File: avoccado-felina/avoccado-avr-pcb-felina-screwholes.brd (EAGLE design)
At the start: 44 x 17.5 mm, 80 parts, among them Q1 16MHz, Q2 FET, U1 MPU-6000QFN-24, U2 MCP73831

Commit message: add redundant fiducials near mounting holes, reverse LED and R
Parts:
- added FID5, FID6, FID7, FID8, FID9: FIDUCIALUFIDUCIAL, SparkFun-Aesthetics:MICRO-FIDUCIAL
- moved FID4 44.7 mm to (2.41, 24.5)
- moved R9 3.05 mm to (40.0, 25.1)
- moved D2 2.41 mm to (42.9, 25.0)
- moved FID1 1.27 mm to (2.41, 39.5)
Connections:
- net 5V: now also D2.A; no longer R9.2
- net GND: now also R9.1; no longer D2.C
- net N$3: now also D2.C, R9.2; no longer D2.A, R9.1
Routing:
- net 3.3V: track 167.2 -> 172.3 mm, vias 3 -> 4
- net VBAT: track 35.2 -> 37.1 mm
- net A5: track 20.9 -> 20.2 mm
- net GND: track 212.7 -> 212.2 mm
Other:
- board text added: "DT"
- board text added: "GN"
- board text added: "LIPO"
- board text added: "RX"
- board text added: "TX"
- board text removed: "BAT"
- board text removed: "D"
- board text removed: "R"
- board text removed: "T"

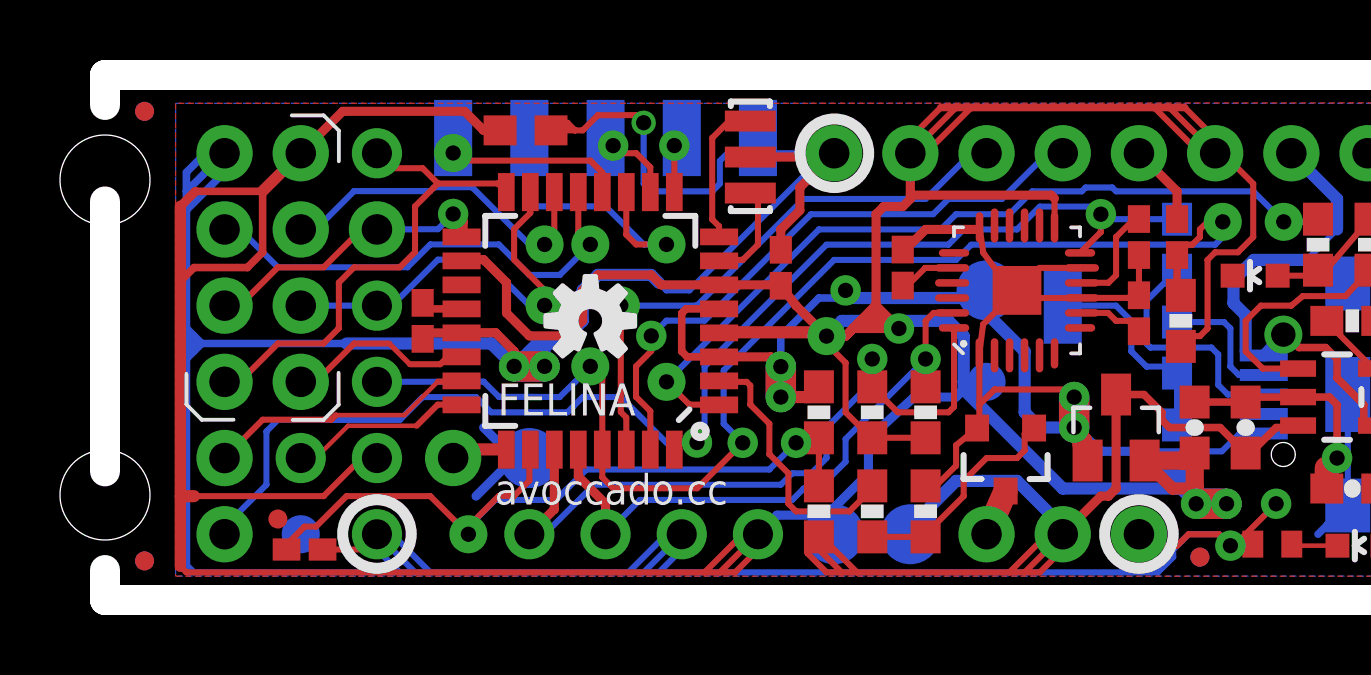
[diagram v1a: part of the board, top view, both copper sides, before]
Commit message: increase trace width for Vcc near edges
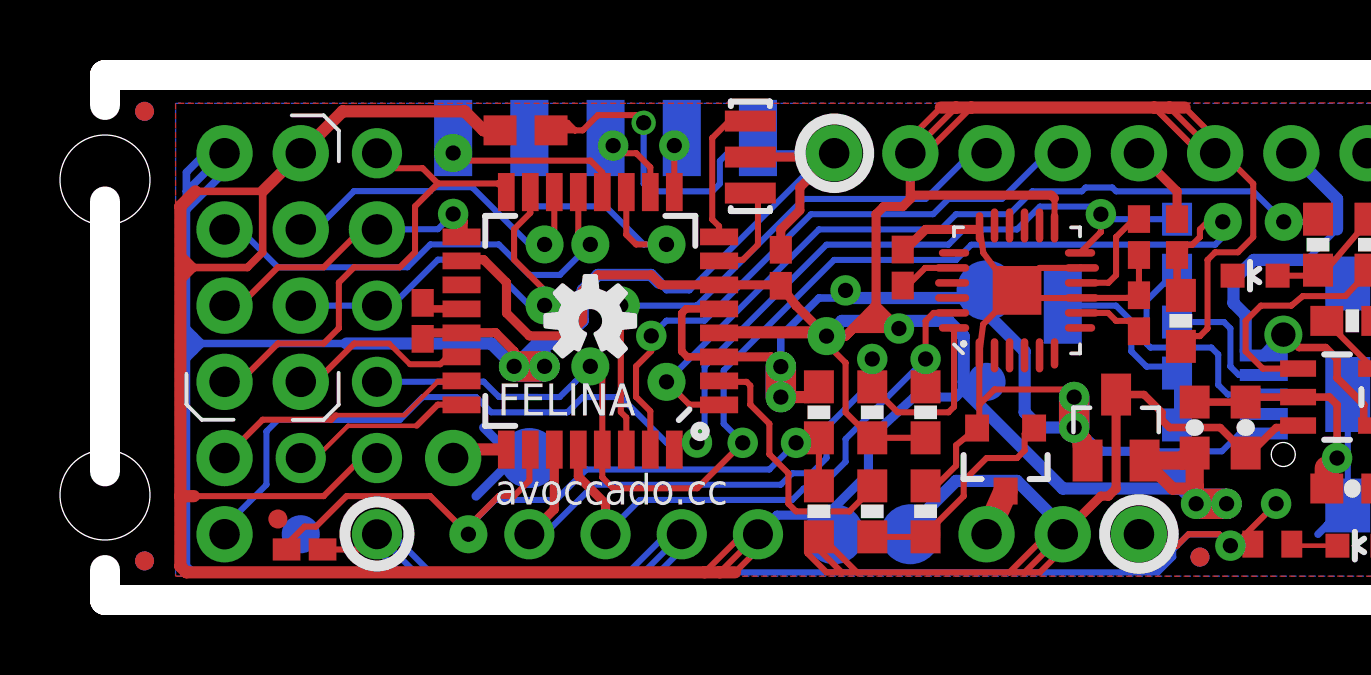
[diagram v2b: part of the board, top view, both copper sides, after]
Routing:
- net 3.3V: track 172.3 -> 173.8 mm
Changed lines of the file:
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@@
 <layer number="22" name="bPlace" color="7" fill="1" visible="yes" active="yes"/>
 <layer number="23" name="tOrigins" color="15" fill="1" visible="yes" active="yes"/>
-<layer number="24" name="bOrigins" color="15" fill="1" visible="yes" active="yes"/>
+<layer number="24" name="bOrigins" color="15" fill="1" visible="no" active="yes"/>
 <layer number="25" name="tNames" color="7" fill="1" visible="no" active="yes"/>
 <layer number="26" name="bNames" color="7" fill="1" visible="no" active="yes"/>
@@
 <layer number="28" name="bValues" color="7" fill="1" visible="no" active="yes"/>
 <layer number="29" name="tStop" color="7" fill="3" visible="yes" active="yes"/>
-<layer number="30" name="bStop" color="7" fill="6" visible="yes" active="yes"/>
-<layer number="31" name="tCream" color="7" fill="4" visible="no" active="yes"/>
-<layer number="32" name="bCream" color="7" fill="5" visible="yes" active="yes"/>
+<layer number="30" name="bStop" color="7" fill="6" visible="no" active="yes"/>
+<layer number="31" name="tCream" color="7" fill="4" visible="yes" active="yes"/>
+<layer number="32" name="bCream" color="7" fill="5" visible="no" active="yes"/>
 <layer number="33" name="tFinish" color="6" fill="3" visible="yes" active="yes"/>
 <layer number="34" name="bFinish" color="6" fill="6" visible="yes" active="yes"/>
@@
 <wire x1="4.326" y1="29.21" x2="5.35" y2="29.21" width="0.127" layer="22"/>
 <rectangle x1="13.208" y1="28.448" x2="21.336" y2="36.576" layer="41"/>
-<circle x="20.32" y="25.408" radius="1.143" width="0.3683" layer="22"/>
+<circle x="20.32" y="25.408" radius="1.0668" width="0.3683" layer="22"/>
 <text x="33.613759375" y="28.141603125" size="1.778" layer="22" font="vector" ratio="15" rot="MR0" align="top-left">+</text>
 <text x="38.956" y="36.576" size="1.016" layer="22" ratio="15" rot="SMR0" align="top-left">VC</text>
@@
 <circle x="25.4" y="38.108" radius="1.143" width="0.3683" layer="22"/>
 <circle x="35.56" y="25.408" radius="1.143" width="0.3683" layer="21"/>
-<circle x="10.16" y="25.408" radius="1.143" width="0.3683" layer="22"/>
-<circle x="10.16" y="25.408" radius="1.143" width="0.3683" layer="21"/>
+<circle x="10.16" y="25.408" radius="1.0668" width="0.3683" layer="22"/>
+<circle x="10.16" y="25.408" radius="1.0668" width="0.3683" layer="21"/>
 <circle x="7.62" y="25.408" radius="0.8128" width="0.3683" layer="22"/>
 <circle x="30.48" y="33.528" radius="1.143" width="0.3683" layer="22"/>
@@
 <wire x1="6.35" y1="36.838" x2="6.35" y2="36.83" width="0.254" layer="1"/>
 <wire x1="6.35" y1="36.83" x2="4.1068" y2="36.83" width="0.254" layer="1"/>
-<wire x1="4.1068" y1="36.83" x2="3.6068" y2="36.33" width="0.3048" layer="1"/>
-<wire x1="3.6068" y1="36.33" x2="3.6068" y2="26.67" width="0.381" layer="1"/>
+<wire x1="4.1068" y1="36.83" x2="3.6068" y2="36.33" width="0.4064" layer="1"/>
+<wire x1="3.6068" y1="36.33" x2="3.6068" y2="26.67" width="0.4064" layer="1"/>
 <contactref element="C6" pad="1"/>
 <contactref element="JP18" pad="1"/>
 <contactref element="JP2" pad="2"/>
-<wire x1="3.6068" y1="26.67" x2="3.6068" y2="24.3332" width="0.381" layer="1"/>
+<wire x1="3.6068" y1="26.67" x2="3.6068" y2="24.3332" width="0.4064" layer="1"/>
 <contactref element="MCU" pad="4"/>
 <contactref element="MCU" pad="6"/>
@@
 <wire x1="6.35" y1="36.83" x2="6.35" y2="34.798" width="0.254" layer="1"/>
 <wire x1="6.35" y1="34.798" x2="5.842" y2="34.29" width="0.254" layer="1"/>
-<wire x1="5.842" y1="34.29" x2="4.064" y2="34.29" width="0.254" layer="1"/>
-<wire x1="4.064" y1="34.29" x2="3.556" y2="33.782" width="0.254" layer="1"/>
-<wire x1="3.556" y1="33.782" x2="3.556" y2="33.528" width="0.254" layer="1"/>
 <contactref element="TP5" pad="P$1"/>
 <wire x1="21.5646" y1="33.712" x2="21.6346" y2="33.782" width="0.254" layer="1"/>
@@
 <wire x1="27.94" y1="36.703" x2="32.639" y2="36.703" width="0.3048" layer="1"/>
 <wire x1="32.639" y1="36.703" x2="32.746" y2="36.596" width="0.3048" layer="1"/>
-<wire x1="3.6068" y1="24.3332" x2="3.81" y2="24.13" width="0.2032" layer="1"/>
-<wire x1="3.81" y1="24.13" x2="21.082" y2="24.13" width="0.2032" layer="1"/>
-<wire x1="21.082" y1="24.13" x2="21.59" y2="24.13" width="0.2032" layer="1"/>
+<wire x1="3.6068" y1="24.3332" x2="3.81" y2="24.13" width="0.4064" layer="1"/>
+<wire x1="3.81" y1="24.13" x2="21.082" y2="24.13" width="0.4064" layer="1"/>
+<wire x1="21.082" y1="24.13" x2="21.59" y2="24.13" width="0.4064" layer="1"/>
 <wire x1="21.59" y1="24.13" x2="22.86" y2="25.4" width="0.2032" layer="1"/>
 <wire x1="3.686234375" y1="26.666765625" x2="4.064" y2="26.67" width="0.4064" layer="1"/>
@@
 <wire x1="3.683" y1="26.67" x2="3.6068" y2="26.67" width="0.2032" layer="1"/>
 <contactref element="JP4" pad="1"/>
-<wire x1="21.59" y1="24.13" x2="22.098" y2="24.13" width="0.2032" layer="1"/>
-<wire x1="14.263" y1="38.862" x2="13.716" y2="38.862" width="0.3048" layer="1"/>
-<wire x1="13.716" y1="38.862" x2="13.081" y2="39.497" width="0.3048" layer="1"/>
-<wire x1="13.081" y1="39.497" x2="9.017" y2="39.497" width="0.3048" layer="1"/>
-<wire x1="9.017" y1="39.497" x2="7.62" y2="38.1" width="0.3048" layer="1"/>
+<wire x1="21.59" y1="24.13" x2="22.098" y2="24.13" width="0.4064" layer="1"/>
+<wire x1="14.263" y1="38.862" x2="13.716" y2="38.862" width="0.4064" layer="1"/>
+<wire x1="13.716" y1="38.862" x2="13.081" y2="39.497" width="0.4064" layer="1"/>
+<wire x1="13.081" y1="39.497" x2="9.017" y2="39.497" width="0.4064" layer="1"/>
+<wire x1="9.017" y1="39.497" x2="7.62" y2="38.1" width="0.4064" layer="1"/>
 <wire x1="22.098" y1="24.13" x2="22.86" y2="24.892" width="0.2032" layer="1"/>
 <wire x1="22.86" y1="24.892" x2="22.86" y2="25.4" width="0.2032" layer="1"/>
@@
 <wire x1="27.94" y1="38.1" x2="28.448" y2="38.1" width="0.254" layer="1"/>
 <wire x1="28.448" y1="38.1" x2="29.972" y2="39.624" width="0.2032" layer="1"/>
-<wire x1="29.464" y1="39.624" x2="28.956" y2="39.624" width="0.254" layer="1"/>
+<wire x1="29.464" y1="39.624" x2="28.956" y2="39.624" width="0.4064" layer="1"/>
 <wire x1="28.956" y1="39.624" x2="27.94" y2="38.608" width="0.2032" layer="1"/>
 <wire x1="27.94" y1="38.608" x2="27.94" y2="38.1" width="0.254" layer="1"/>
-<wire x1="29.464" y1="39.624" x2="29.972" y2="39.624" width="0.254" layer="1"/>
-<wire x1="29.972" y1="39.624" x2="36.068" y2="39.624" width="0.254" layer="1"/>
-<wire x1="36.068" y1="39.624" x2="36.576" y2="39.624" width="0.254" layer="1"/>
+<wire x1="29.464" y1="39.624" x2="29.972" y2="39.624" width="0.4064" layer="1"/>
+<wire x1="29.972" y1="39.624" x2="36.068" y2="39.624" width="0.4064" layer="1"/>
+<wire x1="36.068" y1="39.624" x2="36.576" y2="39.624" width="0.4064" layer="1"/>
 <wire x1="36.576" y1="39.624" x2="38.1" y2="38.1" width="0.2032" layer="1"/>
-<wire x1="36.576" y1="39.624" x2="37.084" y2="39.624" width="0.254" layer="1"/>
+<wire x1="36.576" y1="39.624" x2="37.084" y2="39.624" width="0.4064" layer="1"/>
 <wire x1="37.084" y1="39.624" x2="38.1" y2="38.608" width="0.2032" layer="1"/>
 <wire x1="38.1" y1="38.608" x2="38.1" y2="38.1" width="0.2032" layer="1"/>
@@
 <wire x1="27.559" y1="32.258" x2="26.797" y2="33.02" width="0.3048" layer="1"/>
 <wire x1="26.797" y1="33.02" x2="26.797" y2="32.639" width="0.3048" layer="1"/>
+<wire x1="5.842" y1="34.29" x2="4.064" y2="34.29" width="0.254" layer="1"/>
+<wire x1="4.064" y1="34.29" x2="3.556" y2="33.782" width="0.254" layer="1"/>
+<wire x1="3.556" y1="33.782" x2="3.556" y2="34.29" width="0.254" layer="1"/>
+<wire x1="3.556" y1="34.29" x2="4.064" y2="34.29" width="0.254" layer="1"/>
+<wire x1="4.064" y1="34.29" x2="3.556" y2="34.798" width="0.254" layer="1"/>
 </signal>
 <signal name="D9">

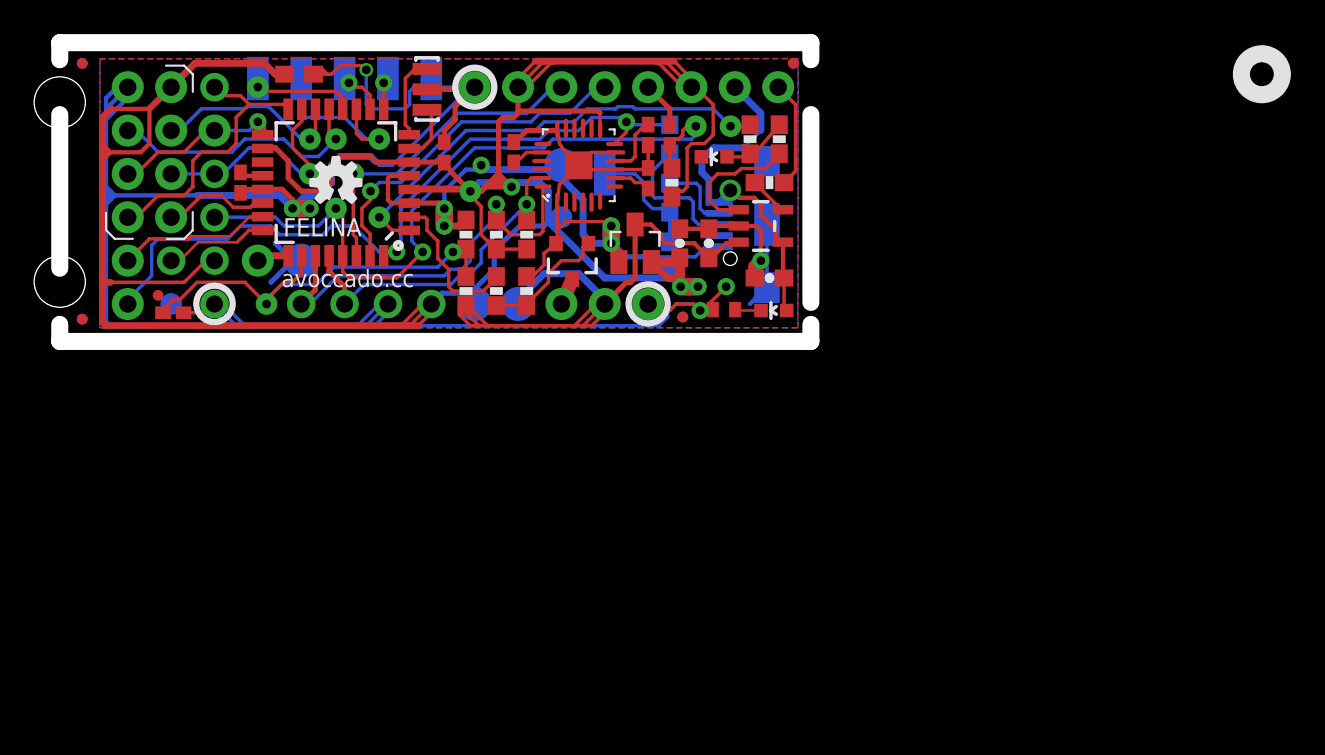
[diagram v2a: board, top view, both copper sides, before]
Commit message: rearrange board for panelization
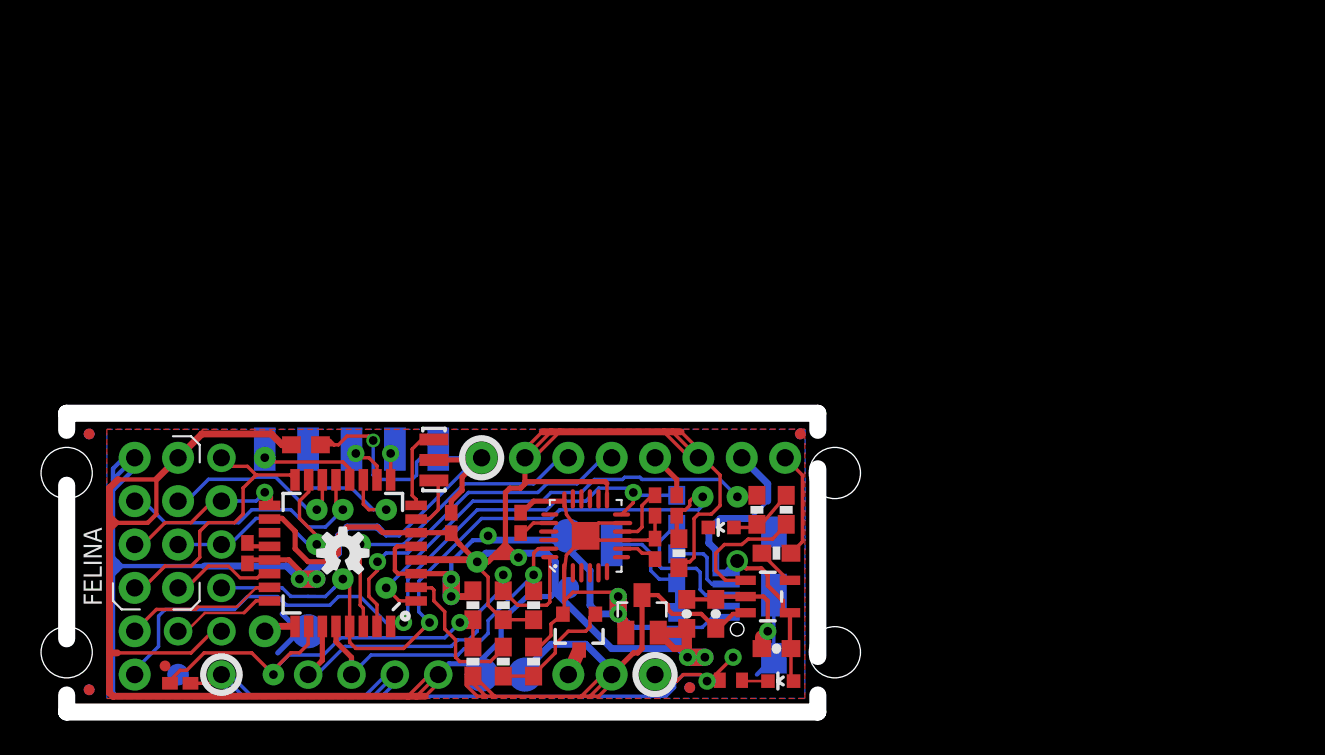
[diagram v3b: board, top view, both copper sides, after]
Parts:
- moved JP14 21.7 mm to (10.6, 11.3)
- moved JP28 21.7 mm to (5.49, 11.3)
- moved TP11 21.7 mm to (33.4, 11.3)
- moved C10 21.7 mm to (15.5, 17.2)
- moved FID3 21.7 mm to (7.26, 4.20)
- moved FID5 21.7 mm to (38.0, 2.93)
- moved FID9 21.7 mm to (38.0, 2.93)
- moved JP10 21.7 mm to (36.0, 16.4)
- moved JP11 21.7 mm to (28.3, 16.4)
- moved JP12 21.7 mm to (10.6, 16.4)
- moved JP13 21.7 mm to (10.6, 13.9)
- moved JP17 21.7 mm to (41.0, 16.4)
- moved JP18 21.7 mm to (38.5, 16.4)
- moved JP19 21.7 mm to (5.49, 6.23)
- moved JP2 21.7 mm to (5.49, 16.4)
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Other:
- outline, holes or cut-outs redrawn
- board text added: "AVOCCADO.CC"
- board text added: "G"
- board text removed: "VB"
- board text removed: "avoccado.cc"
